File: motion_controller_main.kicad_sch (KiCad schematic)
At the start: 321 parts, among them J1 Conn_01x03_Pin, J10 H3, J11 EN4, J12 H4, J13 EN5, J14 H5, J15 EN6, J16 H6, J17 EN7, J18 H7, J19 EN5, J2 EMERGENCY, J20 H5, J21 EN6, J22 H6, J23 EN7, J24 H7, J25 H7, J26 H7, J27 H7, J28 H7, J29 Conn_01x04_Pin, J3 EN0, J30 Conn_01x04_Pin, J31 Conn_01x04_Pin, J32 Conn_01x04_Pin, J33 Conn_01x04_Pin, J34 Conn_01x04_Pin, J35 Conn_01x04_Pin, J36 Conn_01x04_Pin, J37 Conn_01x04_Pin, J38 Conn_01x04_Pin, J39 Conn_01x04_Pin, J4 H0, J40 Conn_01x04_Pin, J41 Conn_01x04_Pin, J42 Conn_01x04_Pin, J43 Conn_01x04_Pin, J44 Conn_01x04_Pin, J45 Conn_01x04_Pin, J46 Conn_01x04_Pin, J47 EMERGENCY, J48 ST-LINK, J49 Inverter, J5 EN1, J50 Conn_01x04_Pin, J51 Conn_01x03_Female, J52 EN5, J53 EN5, J54 Inverter, J55 Conn_01x12_Pin, J57 Conn_01x12_Pin, J58 Conn_01x02_Pin, J59 Conn_01x03_Pin, J6 H1, J60 Conn_01x04_Pin, J7 EN2, J8 H2, J9 EN3, Q1 BCX56, SW3 SW_Push_Dual_x2, SW4 SW_Push_Dual_x2, U1 SN65HVD232D, U10 TLP291-4, U11 TLP291-4, U12 TLP291-4, U13 TLP291-4, U14 TLP291-4, U15 TLP291-4, U16 TLP291-4, U17 ISO7741, U18 ISO7741, U19 ISO7741, U2 STM32F407IGTx, U20 ISO7741, U21 ISO7741, U3 MX25R3235FM2xx1, U30 TLP2372, U31 TLP291, U32 TLP2372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

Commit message: 250806
배선 재배치 + adc + 로드셀 보드 통합 등
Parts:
- removed C51, C52, C53, C54, C55, C56: 1nF, Capacitor_SMD:C_0603_1608Metric_Pad1.08x0.95mm_HandSolder, symbol Device:C
- removed D18, D19, D21, D22, D23: LED, LED_SMD:LED_0805_2012Metric_Pad1.15x1.40mm_HandSolder, symbol Device:LED
- removed J49, J54: Inverter, Connector_Molex:Molex_SPOX_5267-02A_1x02_P2.50mm_Vertical, symbol Connector:Conn_01x02_Pin
- removed J50, J60: Conn_01x04_Pin, Connector_Molex:Molex_SPOX_5267-04A_1x04_P2.50mm_Vertical, symbol Connector:Conn_01x04_Pin
- removed J52, J53: EN5, Connector_Molex:Molex_SPOX_5267-05A_1x05_P2.50mm_Vertical, symbol Connector:Conn_01x05_Pin
- removed J55, J57: Conn_01x12_Pin, Connector_PinHeader_2.54mm:PinHeader_1x12_P2.54mm_Vertical, symbol Connector:Conn_01x12_Pin
- removed JP2, JP3, JP4, JP5, JP6, JP7, JP8, JP9: SolderJumper_2_Open, Jumper:SolderJumper-2_P1.3mm_Open_TrianglePad1.0x1.5mm, symbol Jumper:SolderJumper_2_Open
- removed U22, U23, U24, U25, U26: ~, TMC5160:TMC5160-BOB, symbol tmc5160:tmc5160-bob
- removed U27, U28, U29: ~, TMC5160:TMC5160-CUSTOM, symbol tmc5160:tmc5160-custom
- removed U43: MAX3232, Package_SO:SOIC-16_3.9x9.9mm_P1.27mm, symbol Interface_UART:MAX3232
- added C47, C51, C52, C53, C54, C55, C56: C_Polarized_US, Capacitor_THT:CP_Radial_D8.0mm_P5.00mm, symbol Device:C_Polarized_US
- added C69, C70, C71, C73, C75, C76, C77, C79, C81: 0.1uF, Capacitor_SMD:C_0603_1608Metric, symbol Device:C
- added C72, C78: MF473K, Capacitor_THT:C_Axial_L3.8mm_D2.6mm_P12.50mm_Horizontal, symbol Device:C
- added C74, C80: 1uF, Capacitor_SMD:C_0603_1608Metric, symbol Device:C
- added C82, C83: 0.1uF, Capacitor_SMD:C_0603_1608Metric_Pad1.08x0.95mm_HandSolder, symbol Device:C
- added C84: 2.2uF, Capacitor_Tantalum_SMD:CP_EIA-3216-18_Kemet-A, symbol Device:C_Polarized_US
- added C85, C86: 4.7uF, Capacitor_SMD:C_0603_1608Metric, symbol Device:C
- added D18, D19, D21: M7, Diode_SMD:D_SMA, symbol pspice:DIODE
- added FB1: 600ohm, Inductor_SMD:L_0603_1608Metric, symbol Device:FerriteBead
- added H3, H6, H7, H8, H9: MountingHole, MountingHole:MountingHole_3.2mm_M3, symbol Mechanical:MountingHole
- added IC1: ADM3251EARWZ, SOIC127P1032X265-20N, symbol ADM3251EARWZ:ADM3251EARWZ
- added IC2, IC3: ADS8321E_250, ADS8321:SOP65P490X110-8N, symbol ADS8321E_250:ADS8321E_250
- added J49, J54, J70, J71: Conn_01x03_Pin, Connector_Molex:Molex_SPOX_5267-03A_1x03_P2.50mm_Vertical, symbol Connector:Conn_01x03_Pin
- added J50, J60, J66, J67: EN3, Connector_Molex:Molex_SPOX_5267-05A_1x05_P2.50mm_Vertical, symbol Connector:Conn_01x05_Pin
- added J52, J65: LOADCELL, connectors:SMW250-5, symbol Connector:Conn_01x05_Socket
- added J53, J64: CON2, Connector_Molex:Molex_SPOX_5267-02A_1x02_P2.50mm_Vertical, symbol Connector:Conn_01x02_Pin
- added J55: LOADCELL PWR, connectors:ECH381R-2P, symbol Connector:Conn_01x02_Pin
- added J56, J57, J61, J62, J63, J68: Conn_01x04_Pin, connectors:ECH381R-4P, symbol Connector:Conn_01x04_Pin
- added J69: Conn_01x07_Pin, Connector_PinHeader_2.54mm:PinHeader_1x07_P2.54mm_Vertical, symbol Connector:Conn_01x07_Pin
- added L1: 10uH, Capacitor_SMD:C_1812_4532Metric, symbol Device:L
- added L2: 4.7uH, Inductor_SMD:L_1210_3225Metric, symbol Device:L
- added PS1: NXJ1S0303MC-R13, NXJ1S0303MCR13, symbol NXJ1S0303MC-R13:NXJ1S0303MC-R13
- added Q2, Q3: BCX56, Package_TO_SOT_SMD:SOT-89-3, symbol Transistor_BJT:BCX56
- added R113, R115, R122, R124: 100K 0.1%, Resistor_SMD:R_0805_2012Metric_Pad1.20x1.40mm_HandSolder, symbol Device:R
- added R114, R123: 500 0.1%, Resistor_SMD:R_0805_2012Metric_Pad1.20x1.40mm_HandSolder, symbol Device:R
- added R116, R117, R118, R119, R125, R126, R127, R128: 100 0.1%, Resistor_SMD:R_0603_1608Metric_Pad0.98x0.95mm_HandSolder, symbol Device:R
- added R120, R129: 5, Resistor_SMD:R_0603_1608Metric_Pad0.98x0.95mm_HandSolder, symbol Device:R
- added R121, R130: 100K, Resistor_SMD:R_0603_1608Metric_Pad0.98x0.95mm_HandSolder, symbol Device:R
- added R131, R132, R138, R140, R142, R144, R146, R148, R150, R152, R154, R156, R158, R160: 330, Resistor_SMD:R_0603_1608Metric_Pad0.98x0.95mm_HandSolder, symbol Device:R
- added R133, R134, R137, R139, R141, R143, R145, R147, R149, R151, R153, R155, R157, R159: 1.2k, Resistor_SMD:R_1206_3216Metric, symbol Device:R
- added R135, R136: 4.7K, Resistor_SMD:R_0603_1608Metric_Pad0.98x0.95mm_HandSolder, symbol Device:R
- added R161: 500, Resistor_SMD:R_0805_2012Metric_Pad1.20x1.40mm_HandSolder, symbol Device:R
- added U22, U23, U24, U25, U26, U27, U28, U29, U35, U44, U52: ~, TMC5160:TMC5160-ADT, symbol tmc5160:tmc5160-adt
- added U43, U45: AD8606ARZ, Package_SO:SOIC-8_3.9x4.9mm_P1.27mm, symbol Amplifier_Operational:NCS2325DM
- added U46: ~, Relay_THT:Relay_DPDT_AXICOM_IMSeries_Pitch3.2mm, symbol relay:AGN20012
- added U47: ISO7741, Package_SO:SOIC-16W_7.5x10.3mm_P1.27mm, symbol Isolator:Si8641BC-B-IS1
- added U48, U49, U50: TLP291-4, Package_SO:SOIC-16_4.55x10.3mm_P1.27mm, symbol Isolator:TLP291-4
- added U51: MIC5205-5.0YM5, Package_TO_SOT_SMD:SOT-23-5, symbol Regulator_Linear:MIC5205-5.0YM5
- added X2: TXC-7C, sunny-sco-10:sunny-sco-10, symbol Oscillator:TXC-7C
- C57: value 1nF -> 22uF; footprint Capacitor_SMD:C_0603_1608Metric_Pad1.08x0.95mm_HandSolder -> Capacitor_SMD:C_0805_2012Metric
- C58: value 1nF -> 22pF; footprint Capacitor_SMD:C_0603_1608Metric_Pad1.08x0.95mm_HandSolder -> Capacitor_SMD:C_0603_1608Metric
- C59: value 1nF -> 0.1uF; footprint Capacitor_SMD:C_0603_1608Metric_Pad1.08x0.95mm_HandSolder -> Capacitor_SMD:C_0603_1608Metric
- C60, C61, C62: value 1nF -> 0.1uF 16v; footprint Capacitor_SMD:C_0603_1608Metric_Pad1.08x0.95mm_HandSolder -> Capacitor_SMD:C_0603_1608Metric
- C64: value 0.1uF -> 0.1uF 10v; footprint Capacitor_SMD:C_0603_1608Metric_Pad1.08x0.95mm_HandSolder -> Capacitor_SMD:C_0603_1608Metric
- C65, C66, C67, C68: footprint Capacitor_SMD:C_0603_1608Metric_Pad1.08x0.95mm_HandSolder -> Capacitor_SMD:C_0603_1608Metric
- J47: value EMERGENCY -> SOLVALVE MAIN
- J51: footprint connectors:ECH381R-3P -> Connector_Molex:Molex_SPOX_5267-03A_1x03_P2.50mm_Vertical
- Y1: footprint Crystal:Crystal_HC52-6mm_Vertical -> sunny-sco-10:HC-49SMD
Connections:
- net PA0 is gone; now on net EA0: U2.40 (PA0)
- net PA1 is gone; now on net EB0: U2.41 (PA1)
- net PA2 is gone; now on net EZ0: U2.42 (PA2)
- net +12V: now also J50.2 (Pin_2), J60.2 (Pin_2), J66.2 (Pin_2), J67.2 (Pin_2), R137.2, R139.2, R141.2, R143.2, R145.2, R147.2, R149.2, R151.2, R153.2, R155.2, R157.2, R159.2
- net +24V: now also U36.2 (NC1), R133.2, R134.2, U22.15 (12V), U22.16 (12V), U23.15 (12V), U23.16 (12V), U24.15 (12V), U24.16 (12V), U25.15 (12V), U25.16 (12V), U26.15 (12V), U26.16 (12V), U27.15 (12V), U27.16 (12V), U28.15 (12V), U28.16 (12V), U29.15 (12V), U29.16 (12V), U35.15 (12V), U35.16 (12V), U44.15 (12V), U44.16 (12V), U46.2 (NC1), U46.7 (NC2), U52.15 (12V), U52.16 (12V)
- net +3.3V: now also C24.2, C59.1, R104.1, C83.2, IC1.2 (VCC_1), IC1.3 (VCC_2), J69.1 (Pin_1), J70.2 (Pin_2), J71.2 (Pin_2), L1.1, R136.1, R138.2, R140.2, R142.2, R144.2, R146.2, R148.2, R150.2, R152.2, R154.2, R156.2, R158.2, R160.2, U47.16 (VDD2); no longer C23.2, C65.1, J47.2 (Pin_2), R103.1
- net +3.3VP: now also C82.2, R135.2, U22.3 (3V3), U22.4 (3V3), U23.3 (3V3), U23.4 (3V3), U24.3 (3V3), U24.4 (3V3), U25.3 (3V3), U25.4 (3V3), U26.3 (3V3), U26.4 (3V3), U27.3 (3V3), U27.4 (3V3), U28.3 (3V3), U28.4 (3V3), U29.3 (3V3), U29.4 (3V3), U35.3 (3V3), U35.4 (3V3), U44.3 (3V3), U44.4 (3V3), U47.1 (VDD1), U52.3 (3V3), U52.4 (3V3), X2.1 (EN), X2.4 (Vdd); no longer U36.4 (NO1)
- net A1_0: now also J41.3 (Pin_3), J42.2 (Pin_2), U22.27 (A1), U22.28 (A1); no longer J41.2 (Pin_2), J42.3 (Pin_3)
- net A1_1: now also U23.27 (A1), U23.28 (A1); no longer C57.2
- net A1_2: now also U24.27 (A1), U24.28 (A1); no longer C61.2
- net A2_0: now also J41.4 (Pin_4), J42.1 (Pin_1), U22.29 (A2), U22.30 (A2); no longer J41.1 (Pin_1), J42.4 (Pin_4)
- net A2_1: now also U23.29 (A2), U23.30 (A2); no longer C58.2
- net A2_2: now also U24.29 (A2), U24.30 (A2); no longer C62.2
- net ADC_CS0: now also U2.128 (PH13); no longer U2.131 (PI0)
- net ADC_CS0_O: now also IC2.5 (~{CS}/SHDN)
- net ADC_CS1: now also U2.129 (PH14); no longer U2.128 (PH13)
- net ADC_CS1_O: now also IC3.5 (~{CS}/SHDN)
- net B1_0: now also J41.1 (Pin_1), J42.4 (Pin_4), U22.23 (B1), U22.24 (B1); no longer J41.4 (Pin_4), J42.1 (Pin_1)
- net B1_1: now also U23.23 (B1), U23.24 (B1)
- net B1_2: now also U24.23 (B1), U24.24 (B1); no longer C59.2
- net B2_0: now also J41.2 (Pin_2), J42.3 (Pin_3), U22.25 (B2), U22.26 (B2); no longer J41.3 (Pin_3), J42.2 (Pin_2)
- net B2_1: now also U23.25 (B2), U23.26 (B2)
- net B2_2: now also U24.25 (B2), U24.26 (B2); no longer C60.2
- net BUZZER: now also U2.8 (PC13); no longer U2.50 (PA4)
- net CAN1H: now also J49.3 (Pin_3), J54.3 (Pin_3)
- net CAN1L: now also J49.2 (Pin_2), J54.2 (Pin_2)
- net CS0: now also U2.175 (PI6), U47.11 (B4); no longer U18.5 (A3), U2.1 (PE2)
- net CS0_O: now also U22.1 (CSN), U47.6 (A4), U52.1 (CSN); no longer U18.12 (B3)
- net CS1: now also U19.11 (B4), U2.169 (PE0); no longer U18.4 (A2), U2.4 (PE5)
- net CS1_O: now also U19.6 (A4), U23.1 (CSN); no longer U18.13 (B2)
- net CS2: now also U2.154 (PG11); no longer U2.8 (PC13)
- net CS2_O: now also U24.1 (CSN)
- net CS3: now also U18.4 (A2), U2.153 (PG10); no longer U2.173 (PI4), U20.3 (A1)
- net CS3_O: now also U18.13 (B2), U25.1 (CSN); no longer U20.14 (B1)
- net CS4: now also U18.5 (A3), U2.152 (PG9); no longer U2.168 (PB9), U20.4 (A2)
- net CS4_O: now also U18.12 (B3), U26.1 (CSN); no longer U20.13 (B2)
- net CS5: now also U2.150 (PD6), U20.3 (A1); no longer U2.164 (PB6), U20.5 (A3)
- net CS5_O: now also U20.14 (B1), U27.1 (CSN); no longer U20.12 (B3)
- net CS6: now also U2.146 (PD4), U20.4 (A2); no longer U17.5 (A3), U2.156 (PG13)
- net CS6_O: now also U20.13 (B2), U28.1 (CSN); no longer U17.12 (B3)
- net CS7: now also U2.145 (PD3), U20.5 (A3); no longer U2.153 (PG10), U21.11 (B4)
- net CS7_O: now also U20.12 (B3), U29.1 (CSN); no longer U21.6 (A4)
- net DIAG0_0: now also U2.174 (PI5), U47.12 (B3); no longer U19.12 (B3), U2.47 (PA3)
- net DIAG0_0_O: now also U22.2 (DIAG0), U47.5 (A3); no longer D16.2 (A), U19.5 (A3)
- net DIAG0_1: now also U2.173 (PI4), U47.13 (B2); no longer U19.13 (B2), U2.46 (PH5)
- net DIAG0_1_O: now also U23.2 (DIAG0), U47.4 (A2); no longer D17.2 (A), U19.4 (A2)
- net DIAG0_2: now also U19.12 (B3), U2.168 (PB9); no longer U19.14 (B1), U2.45 (PH4)
- net DIAG0_2_O: now also U19.5 (A3), U24.2 (DIAG0); no longer U19.3 (A1)
- net DIAG0_3: now also U19.13 (B2), U2.167 (PB8); no longer U2.146 (PD4), U21.14 (B1)
- net DIAG0_3_O: now also U19.4 (A2), U25.2 (DIAG0); no longer U21.3 (A1)
- net DIAG0_4: now also U19.14 (B1), U2.155 (PG12); no longer U2.147 (PD5), U21.13 (B2)
- net DIAG0_4_O: now also U19.3 (A1), U26.2 (DIAG0); no longer D20.2 (A), U21.4 (A2)
- net DIAG0_5: now also U18.6 (A4), U2.151 (PD7); no longer U2.150 (PD6), U21.12 (B3)
- net DIAG0_5_O: now also U18.11 (B4), U27.2 (DIAG0); no longer U21.5 (A3)
- net DIAG0_6: now also U2.143 (PD1); no longer U2.151 (PD7)
- net DIAG0_6_O: now also U28.2 (DIAG0)
- net DIAG0_7: now also U2.141 (PC12), U21.12 (B3); no longer U18.6 (A4), U2.152 (PG9)
- net DIAG0_7_O: now also U21.5 (A3), U29.2 (DIAG0); no longer U18.11 (B4)
- net DRV_ENN_O: now also U22.10 (DRV_ENN), U23.10 (DRV_ENN), U24.10 (DRV_ENN), U25.10 (DRV_ENN), U26.10 (DRV_ENN), U27.10 (DRV_ENN), U28.10 (DRV_ENN), U29.10 (DRV_ENN), U35.10 (DRV_ENN), U44.10 (DRV_ENN), U52.10 (DRV_ENN); no longer U36.3 (COM1)
- net EA0: no longer U2.54 (PC4)
- net EB0: no longer U2.55 (PC5)
- net EMERGENCY: now also U2.176 (PI7); no longer U2.174 (PI5)
- net EZ0: no longer U2.56 (PB0)
- net GND: now also C24.1, C57.1, C59.2, C83.1, IC1.10 (GND_5), IC1.4 (GND_1), IC1.5 (GND_2), IC1.6 (GND_3), IC1.7 (GND_4), J49.1 (Pin_1), J54.1 (Pin_1), J69.2 (Pin_2), J70.1 (Pin_1), J71.1 (Pin_1), PS1.1 (-VIN), U47.15 (GND2), U47.9 (GND2), U48.11, U48.13, U48.15, U48.9, U49.11, U49.13, U49.15, U49.9, U50.11, U50.13, U50.15, U50.9; no longer C23.1, C65.2, C67.2, C68.2, J47.1 (Pin_1), J59.3 (Pin_3)
- net GND1: now also J50.1 (Pin_1), J60.1 (Pin_1), J66.1 (Pin_1), J67.1 (Pin_1), U48.2, U48.4, U48.6, U48.8, U49.2, U49.4, U49.6, U49.8, U50.2, U50.4, U50.6, U50.8
- net GND2: now also J47.2 (Pin_2), U36.4 (NO1), C47.2, C51.2, C52.2, C53.2, C54.2, C55.2, C56.2, C82.1, D21.1 (K), Q2.3 (E), Q3.3 (E), U22.11 (GND), U22.12 (GND), U22.13 (GND), U22.14 (GND), U22.8 (GND), U23.11 (GND), U23.12 (GND), U23.13 (GND), U23.14 (GND), U23.6 (CLK16), U23.8 (GND), U24.11 (GND), U24.12 (GND), U24.13 (GND), U24.14 (GND), U24.6 (CLK16), U24.8 (GND), U25.11 (GND), U25.12 (GND), U25.13 (GND), U25.14 (GND), U25.6 (CLK16), U25.8 (GND), U26.11 (GND), U26.12 (GND), U26.13 (GND), U26.14 (GND), U26.6 (CLK16), U26.8 (GND), U27.11 (GND), U27.12 (GND), U27.13 (GND), U27.14 (GND), U27.6 (CLK16), U27.8 (GND), U28.11 (GND), U28.12 (GND), U28.13 (GND), U28.14 (GND), U28.6 (CLK16), U28.8 (GND), U29.11 (GND), U29.12 (GND), U29.13 (GND), U29.14 (GND), U29.6 (CLK16), U29.8 (GND), U35.11 (GND), U35.12 (GND), U35.13 (GND), U35.14 (GND), U35.6 (CLK16), U35.8 (GND), U44.11 (GND), U44.12 (GND), U44.13 (GND), U44.14 (GND), U44.6 (CLK16), U44.8 (GND), U46.4 (NO1), U46.5 (NO2), U46.8 (-), U47.2 (GND1), U47.8 (GND1), U52.11 (GND), U52.12 (GND), U52.13 (GND), U52.14 (GND), U52.8 (GND), X2.2 (GND); no longer C57.1, C58.1, C59.1, C60.1, C61.1, C62.1, U36.2 (NC1)
- net GNDS: now also C23.1, D20.1 (K), C73.2, C74.2, C75.2, C79.2, C80.2, C81.2, C84.2, C85.1, C86.2, IC2.4 (GND), IC3.4 (GND), J52.1 (Pin_1), J55.1 (Pin_1), J65.1 (Pin_1), R119.2, R121.2, R128.2, R130.2, U43.4 (V-), U45.4 (V-), U51.2 (GND); no longer C24.1
- net INVERTER0: now also D17.2 (A); no longer U38.1
- net INVERTER1: now also D16.2 (A), U2.131 (PI0); no longer U2.129 (PH14), U41.1
- net RS232_RX: now also IC1.15 (RIN)
- net RS232_TX: now also IC1.16 (TOUT)
- net SPI2_MISO_O: now also IC2.6 (DOUT), IC3.6 (DOUT)
- net SPI2_SCK_O: now also IC2.7 (DCLOCK), IC3.7 (DCLOCK)
- net SPI3_MISO_O: now also U22.5 (MISO), U23.5 (MISO), U24.5 (MISO), U25.5 (MISO), U26.5 (MISO), U27.5 (MISO), U28.5 (MISO), U29.5 (MISO), U35.5 (MISO), U44.5 (MISO), U52.5 (MISO)
- net SPI3_MOSI_O: now also U22.7 (MOSI), U23.7 (MOSI), U24.7 (MOSI), U25.7 (MOSI), U26.7 (MOSI), U27.7 (MOSI), U28.7 (MOSI), U29.7 (MOSI), U35.7 (MOSI), U44.7 (MOSI), U52.7 (MOSI)
- net SPI3_SCK_O: now also U22.9 (SCK), U23.9 (SCK), U24.9 (SCK), U25.9 (SCK), U26.9 (SCK), U27.9 (SCK), U28.9 (SCK), U29.9 (SCK), U35.9 (SCK), U44.9 (SCK), U52.9 (SCK)
- net USART1_RX: now also IC1.8 (ROUT)
- net USART1_TX: now also IC1.9 (TIN)
- net VPP: now also C47.1, C51.1, C52.1, C53.1, C54.1, C55.1, C56.1, U22.17 (60V), U22.18 (60V), U22.19 (60V), U22.20 (60V), U22.21 (60V), U22.22 (60V), U23.17 (60V), U23.18 (60V), U23.19 (60V), U23.20 (60V), U23.21 (60V), U23.22 (60V), U24.17 (60V), U24.18 (60V), U24.19 (60V), U24.20 (60V), U24.21 (60V), U24.22 (60V), U25.17 (60V), U25.18 (60V), U25.19 (60V), U25.20 (60V), U25.21 (60V), U25.22 (60V), U26.17 (60V), U26.18 (60V), U26.19 (60V), U26.20 (60V), U26.21 (60V), U26.22 (60V), U27.17 (60V), U27.18 (60V), U27.19 (60V), U27.20 (60V), U27.21 (60V), U27.22 (60V), U28.17 (60V), U28.18 (60V), U28.19 (60V), U28.20 (60V), U28.21 (60V), U28.22 (60V), U29.17 (60V), U29.18 (60V), U29.19 (60V), U29.20 (60V), U29.21 (60V), U29.22 (60V), U35.17 (60V), U35.18 (60V), U35.19 (60V), U35.20 (60V), U35.21 (60V), U35.22 (60V), U44.17 (60V), U44.18 (60V), U44.19 (60V), U44.20 (60V), U44.21 (60V), U44.22 (60V), U52.17 (60V), U52.18 (60V), U52.19 (60V), U52.20 (60V), U52.21 (60V), U52.22 (60V)
- net B1_3: now reaches J31.1 (Pin_1)
- net B1_3: now also J32.4 (Pin_4), U25.23 (B1), U25.24 (B1); no longer J40.4 (Pin_4)
- net B2_3: now reaches J31.2 (Pin_2)
- net B2_3: now also J32.3 (Pin_3), U25.25 (B2), U25.26 (B2); no longer J40.3 (Pin_3)
- net A1_3: now reaches J31.3 (Pin_3)
- net A1_3: now also J32.2 (Pin_2), U25.27 (A1), U25.28 (A1); no longer J40.2 (Pin_2)
- net A2_3: now reaches J31.4 (Pin_4)
- net A2_3: now also J32.1 (Pin_1), U25.29 (A2), U25.30 (A2); no longer J40.1 (Pin_1)
- net at U40.10 (EN2): now also R103.2; no longer R104.2
- net at U40.7 (EN1): now also R104.2; no longer R103.2
- net B1_4: now reaches J34.4 (Pin_4)
- net B1_4: now also J33.1 (Pin_1), U26.23 (B1), U26.24 (B1); no longer J37.1 (Pin_1)
- net B2_4: now reaches J34.3 (Pin_3)
- net B2_4: now also J33.2 (Pin_2), U26.25 (B2), U26.26 (B2); no longer J37.2 (Pin_2)
- net A1_4: now reaches J34.2 (Pin_2)
- net A1_4: now also J33.3 (Pin_3), U26.27 (A1), U26.28 (A1); no longer J37.3 (Pin_3)
- net A2_4: now reaches J34.1 (Pin_1)
- net A2_4: now also J33.4 (Pin_4), U26.29 (A2), U26.30 (A2); no longer J37.4 (Pin_4)
- net EB12: now reaches U2.13 (PI11)
- net EB12: now also R146.1, U49.16
- net DIAG0_9: now reaches U2.139 (PC10)
- net DIAG0_9: now also U21.14 (B1)
- net DIAG0_8: now reaches U2.140 (PC11)
- net DIAG0_8: now also U21.13 (B2)
- net CS9: now reaches U2.142 (PD0)
- net CS9: now also U21.11 (B4)
- net CS8: now reaches U2.144 (PD2)
- net CS8: now also U17.5 (A3)
- net DIAG0_11: now reaches U2.170 (PE1)
- net DIAG0_11: now also U47.14 (B1)
- net PE3: now reaches U2.2 (PE3)
- net PE3: now also J69.4 (Pin_4)
- net PE4: now reaches U2.3 (PE4)
- net PE4: now also J69.5 (Pin_5)
- net PE6: now reaches U2.5 (PE6)
- net PE6: now also J69.7 (Pin_7)
- net EMERGENCY_O: now reaches J2.1 (Pin_1), U36.1 (+)
- net EMERGENCY_O: now also U46.1 (+)
- net B1_7: now reaches J39.1 (Pin_1)
- net B1_7: now also J40.4 (Pin_4), U29.23 (B1), U29.24 (B1); no longer J32.4 (Pin_4)
- net B2_7: now reaches J39.2 (Pin_2)
- net B2_7: now also J40.3 (Pin_3), U29.25 (B2), U29.26 (B2); no longer J32.3 (Pin_3)
- net A1_7: now reaches J39.3 (Pin_3)
- net A1_7: now also J40.2 (Pin_2), U29.27 (A1), U29.28 (A1); no longer J32.2 (Pin_2)
- net A2_7: now reaches J39.4 (Pin_4)
- net A2_7: now also J40.1 (Pin_1), U29.29 (A2), U29.30 (A2); no longer J32.1 (Pin_1)
- net at U41.3: now also Q2.1 (B)
- net at U41.4: now also R133.1
- net at U38.3: now also Q3.1 (B)
- net at U38.4: now also R134.1
- net at C64.1: now also IC1.19 (V+)
- net +3.3ISO: now reaches C64.2
- net +3.3ISO: now also C58.2, C65.2, IC1.20 (VISO), L2.2
- net at D16.1 (K): now also R131.2
- net at D17.1 (K): now also R132.2
- net B1_6: now reaches J38.4 (Pin_4)
- net B1_6: now also J37.1 (Pin_1), U28.23 (B1), U28.24 (B1); no longer J33.1 (Pin_1)
- net B2_6: now reaches J38.3 (Pin_3)
- net B2_6: now also J37.2 (Pin_2), U28.25 (B2), U28.26 (B2); no longer J33.2 (Pin_2)
- net A1_6: now reaches J38.2 (Pin_2)
- net A1_6: now also J37.3 (Pin_3), U28.27 (A1), U28.28 (A1); no longer J33.3 (Pin_3)
- net A2_6: now reaches J38.1 (Pin_1)
- net A2_6: now also J37.4 (Pin_4), U28.29 (A2), U28.30 (A2); no longer J33.4 (Pin_4)
- net B1_5: now reaches J35.1 (Pin_1), J36.4 (Pin_4)
- net B1_5: now also U27.23 (B1), U27.24 (B1)
- net B2_5: now reaches J35.2 (Pin_2), J36.3 (Pin_3)
- net B2_5: now also U27.25 (B2), U27.26 (B2)
- net A1_5: now reaches J35.3 (Pin_3), J36.2 (Pin_2)
- net A1_5: now also U27.27 (A1), U27.28 (A1)
- net A2_5: now reaches J35.4 (Pin_4), J36.1 (Pin_1)
- net A2_5: now also U27.29 (A2), U27.30 (A2)
- net at C67.1: now also C77.1, R123.1, R124.2, U45.6 (-)
- net at C66.2: now also C76.2, R122.1, R123.2, U45.2 (-)
- net at C66.1: now also C76.1, R122.2, R125.1, U45.1
- net at C68.1: now also C70.1, R113.2, R116.1, U43.1
- removed net +3V3: C24.2, R104.1, U40.16 (VDD2)
- net PC14 renamed EZ11
- net EZ11: now also R138.1, U48.16
- net PC15 renamed EB11
- net EB11: now also R140.1, U48.14
- net PF0 renamed EA12
- net EA12: now also R148.1, U49.14
- net PF1: no longer names the net of U2.17 (PF1)
- net PF10 renamed EA14
- net EA14: now also R160.1, U50.10
- net PF2 renamed EZ13
- net EZ13: now also R150.1, U49.12
- net PF3 renamed EB13
- net EB13: now also R152.1, U49.10
- net PF4 renamed EA13
- net EA13: now also R154.1, U50.16
- net PF5: no longer names the net of U2.21 (PF5)
- net PF6: no longer names the net of U2.24 (PF6)
- net PF7: no longer names the net of U2.25 (PF7)
- net PF8 renamed EZ14
- net EZ14: now also R156.1, U50.14
- net PF9 renamed EB14
- net EB14: now also R158.1, U50.12
- net PH2: no longer names the net of U2.43 (PH2)
- net PH3: no longer names the net of U2.44 (PH3)
- net PI10 renamed EZ12
- net EZ12: now also R144.1, U48.10
- net PI9 renamed EA11
- net EA11: now also R142.1, U48.12
- new net: C81.1, J52.5 (Pin_5), R130.1
- new net: D18.1 (K), J53.1 (Pin_1), Q2.2 (C)
- new net: C78.2, IC3.2 (+IN), R125.2
- new net: C74.1, IC2.8 (+VCC), R120.2
- new net: C69.1, C71.1, R114.1, R115.2, U43.6 (-)
- new net: C69.2, C71.2, R115.1, R117.1, U43.7
- new net: C67.2, C77.2, R124.1, R126.1, U45.7
- new net: C68.2, C70.2, R113.1, R114.2, U43.2 (-)
- new net: C72.1, IC2.3 (-IN), R117.2
- new net: C80.1, IC3.8 (+VCC), R129.2
- new net: C78.1, IC3.3 (-IN), R126.2
- new net: C60.1, IC1.18 (C1+)
- new net: C60.2, IC1.17 (C1-)
- new net: D19.1 (K), J64.1 (Pin_1), Q3.2 (C)
- new net: R136.2, U47.10 (EN2)
- new net: R135.1, U47.7 (EN1)
- new net: R132.1, U38.1
- new net: C72.2, IC2.2 (+IN), R116.2
- new net: C79.1, IC3.1 (VREF), R127.2, R128.1
- new net: C73.1, IC2.1 (VREF), R118.2, R119.1
- new net: C57.2, L1.2, PS1.3 (+VIN)
- new net: L2.1, PS1.8 (+VOUT)
- new net: C86.1, FB1.2, U51.1 (IN)
- new net: D20.2 (A), R161.1
- new net: R131.1, U41.1
- new net: C62.1, IC1.12 (V-)
- new net: C61.2, IC1.13 (C2-)
- new net: C61.1, IC1.14 (C2+)
- new net: C85.2, U51.4 (BP)
- new net: C75.1, J65.5 (Pin_5), R121.1
- new net +5V: C23.2, C84.1, J52.2 (Pin_2), J65.2 (Pin_2), R103.1, R118.1, R120.1, R127.1, R129.1, R161.2, U40.16 (VDD2), U43.8 (V+), U45.8 (V+), U51.5 (OUT)
- new net +5V5: FB1.1, J55.2 (Pin_2), U51.3 (EN)
- new net 16MHz: U22.6 (CLK16), U52.6 (CLK16), X2.3 (OUT)
- new net A1_11: J57.3 (Pin_3), J68.2 (Pin_2), U52.27 (A1), U52.28 (A1)
- new net A1_8: J56.3 (Pin_3), J61.2 (Pin_2), U35.27 (A1), U35.28 (A1)
- new net A1_9: J62.3 (Pin_3), J63.2 (Pin_2), U44.27 (A1), U44.28 (A1)
- new net A2_11: J57.4 (Pin_4), J68.1 (Pin_1), U52.29 (A2), U52.30 (A2)
- new net A2_8: J56.4 (Pin_4), J61.1 (Pin_1), U35.29 (A2), U35.30 (A2)
- new net A2_9: J62.4 (Pin_4), J63.1 (Pin_1), U44.29 (A2), U44.30 (A2)
- new net ADC1_IN14: J71.3 (Pin_3), U2.54 (PC4)
- new net ADC1_IN15: J70.3 (Pin_3), U2.55 (PC5)
- new net B1_11: J57.1 (Pin_1), J68.4 (Pin_4), U52.23 (B1), U52.24 (B1)
- new net B1_8: J56.1 (Pin_1), J61.4 (Pin_4), U35.23 (B1), U35.24 (B1)
- new net B1_9: J62.1 (Pin_1), J63.4 (Pin_4), U44.23 (B1), U44.24 (B1)
- new net B2_11: J57.2 (Pin_2), J68.3 (Pin_3), U52.25 (B2), U52.26 (B2)
- new net B2_8: J56.2 (Pin_2), J61.3 (Pin_3), U35.25 (B2), U35.26 (B2)
- new net B2_9: J62.2 (Pin_2), J63.3 (Pin_3), U44.25 (B2), U44.26 (B2)
- new net CS8_O: U17.12 (B3), U35.1 (CSN)
- new net CS9_O: U21.6 (A4), U44.1 (CSN)
- new net DIAG0_11_O: U47.3 (A1), U52.2 (DIAG0)
- new net DIAG0_8_O: U21.4 (A2), U35.2 (DIAG0)
- new net DIAG0_9_O: U21.3 (A1), U44.2 (DIAG0)
- new net GND3: C58.1, C62.2, C65.1, IC1.11 (GNDISO), J59.3 (Pin_3), PS1.7 (-VOUT)
- new net INVERTER0_O: D19.2 (A), J64.2 (Pin_2), U46.6 (COM2)
- new net INVERTER1_O: D18.2 (A), J53.2 (Pin_2), U46.3 (COM1)
- new net PE2: J69.3 (Pin_3), U2.1 (PE2)
- new net PE5: J69.6 (Pin_6), U2.4 (PE5)
- new net S0+: J65.4 (Pin_4), U43.3 (+)
- new net S0-: J65.3 (Pin_3), U43.5 (+)
- new net S1+: J52.4 (Pin_4), U45.3 (+)
- new net S1-: J52.3 (Pin_3), U45.5 (+)
- new net SOLVALVE_MAIN: D21.2 (A), J47.1 (Pin_1), U36.3 (COM1)
- new net S_EA11: J50.5 (Pin_5), R141.1, U48.5
- new net S_EA12: J60.5 (Pin_5), R147.1, U49.3
- new net S_EA13: J66.5 (Pin_5), R153.1, U50.1
- new net S_EA14: J67.5 (Pin_5), R159.1, U50.7
- new net S_EB11: J50.4 (Pin_4), R139.1, U48.3
- new net S_EB12: J60.4 (Pin_4), R145.1, U49.1
- new net S_EB13: J66.4 (Pin_4), R151.1, U49.7
- new net S_EB14: J67.4 (Pin_4), R157.1, U50.5
- new net S_EZ11: J50.3 (Pin_3), R137.1, U48.1
- new net S_EZ12: J60.3 (Pin_3), R143.1, U48.7
- new net S_EZ13: J66.3 (Pin_3), R149.1, U49.5
- new net S_EZ14: J67.3 (Pin_3), R155.1, U50.3
- no-connect marks 36 -> 0
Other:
- note added: "ADC"
- note added: "RS232"
- moved on the sheet: C16, C27, C28, C29, C30, C31, C32, C33, C34, C35, C48, C49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

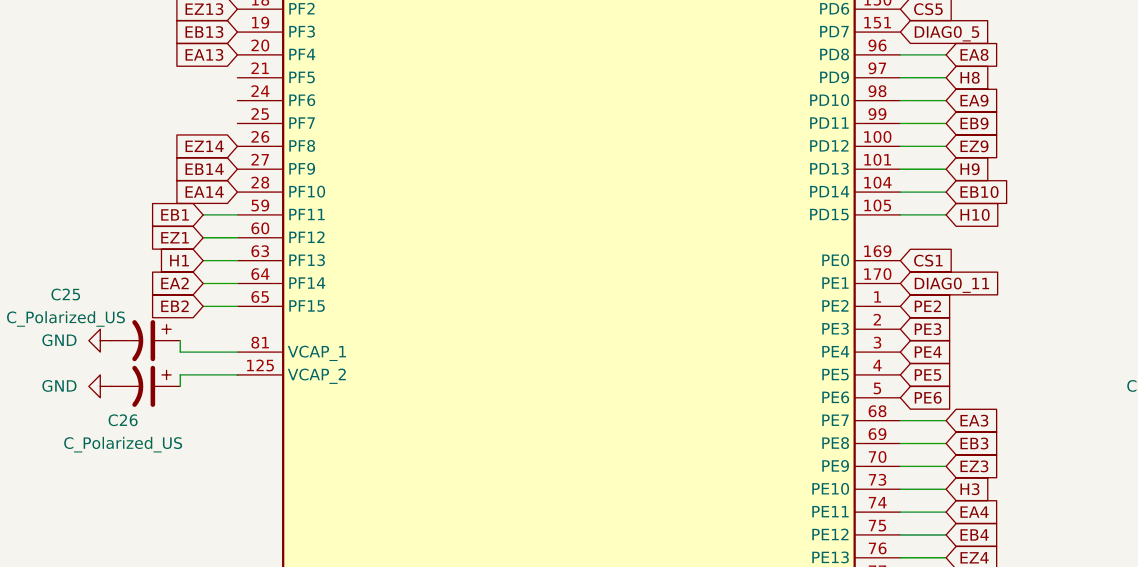
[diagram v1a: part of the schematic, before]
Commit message: 250825
E14A핀 연결 불량 처리 PE5못씀
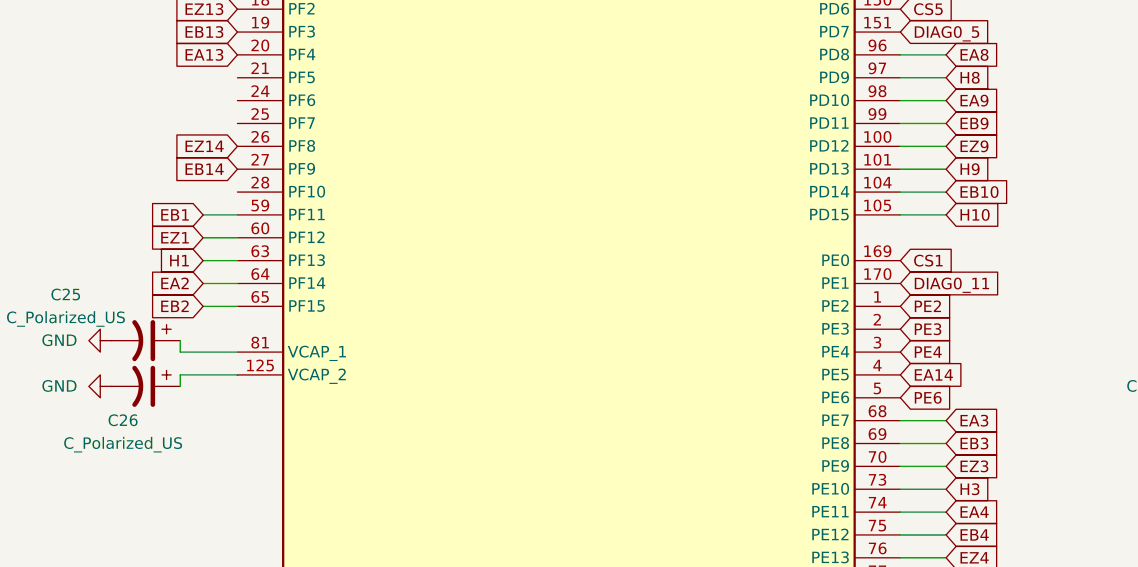
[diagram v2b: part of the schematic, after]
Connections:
- net EA14: now also U2.4 (PE5); no longer U2.28 (PF10)
- net PE5: no longer U2.4 (PE5)
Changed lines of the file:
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@@
 		)
 	)
-	(global_label "PE5"
+	(global_label "A2_8"
+		(shape input)
+		(at 819.15 699.77 0)
+		(fields_autoplaced yes)
+		(effects
+			(font
+				(size 1.27 1.27)
+			)
+			(justify left)
+		)
+		(property "Intersheetrefs" "${INTERSHEET_REFS}"
+			(at 826.6104 699.77 0)
+			(effects
+				(font
+					(size 1.27 1.27)
+				)
+				(justify left)
+				(hide yes)
+			)
+		)
+	)
+	(global_label "EA1"
+		(shape input)
+		(at 143.51 426.72 180)
+		(fields_autoplaced yes)
+		(effects
+			(font
+				(size 1.27 1.27)
+			)
+			(justify right)
+		)
+		(property "Intersheetrefs" "${INTERSHEET_REFS}"
+			(at 137.0777 426.72 0)
+			(effects
+				(font
+					(size 1.27 1.27)
+				)
+				(justify right)
+				(hide yes)
+			)
+		)
+	)
+	(global_label "EA14"
 		(shape input)
 		(at 469.9 289.56 0)
@@
 		)
 		(property "Intersheetrefs" "${INTERSHEET_REFS}"
-			(at 476.5137 289.56 0)
-			(effects
-				(font
-					(size 1.27 1.27)
-				)
-				(justify left)
-				(hide yes)
-			)
-		)
-	)
-	(global_label "A2_8"
-		(shape input)
-		(at 819.15 699.77 0)
-		(fields_autoplaced yes)
-		(effects
-			(font
-				(size 1.27 1.27)
-			)
-			(justify left)
-		)
-		(property "Intersheetrefs" "${INTERSHEET_REFS}"
-			(at 826.6104 699.77 0)
-			(effects
-				(font
-					(size 1.27 1.27)
-				)
-				(justify left)
-				(hide yes)
-			)
-		)
-	)
-	(global_label "EA1"
-		(shape input)
-		(at 143.51 426.72 180)
-		(fields_autoplaced yes)
-		(effects
-			(font
-				(size 1.27 1.27)
-			)
-			(justify right)
-		)
-		(property "Intersheetrefs" "${INTERSHEET_REFS}"
-			(at 137.0777 426.72 0)
-			(effects
-				(font
-					(size 1.27 1.27)
-				)
-				(justify right)
+			(at 477.5418 289.56 0)
+			(effects
+				(font
+					(size 1.27 1.27)
+				)
+				(justify left)
 				(hide yes)
 			)
@@
 				(hide yes)
 			)
-		)
-	)
-	(global_label "EA14"
-		(shape input)
-		(at 396.24 269.24 180)
-		(fields_autoplaced yes)
-		(effects
-			(font
-				(size 1.27 1.27)
-			)
-			(justify right)
-		)
-		(property "Intersheetrefs" "${INTERSHEET_REFS}"
-			(at 388.5982 269.24 0)
-			(effects
-				(font
-					(size 1.27 1.27)
-				)
-				(justify right)
-				(hide yes)
-			)

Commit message: 251022
gpio확인 pe5가 없어서 커넥터 수정
무라타 보드에서 인덕터 안쓰는거 대비 솔더브릿지 추가
캐패시터 24와 60중 고를 수 있게 수정 해야함
diag led가 빠졌는데 추가할지 확인해야함
병렬모터 spi 읽기 충돌 방지 대책 세워야 함
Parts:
- added JP2: SolderJumper_2_Open, Jumper:SolderJumper-2_P1.3mm_Open_TrianglePad1.0x1.5mm, symbol Jumper:SolderJumper_2_Open
- C58: value 22pF -> 22uF 22pF x 22uF ok; footprint Capacitor_SMD:C_0603_1608Metric -> Capacitor_SMD:C_0805_2012Metric
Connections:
- net PE5 is gone; now on net PE6: J69.6 (Pin_6)
- net +3.3ISO: now also JP2.1 (A)
- net GND: now also J69.7 (Pin_7)
- net PE6: no longer J69.7 (Pin_7)
- net at L2.1, PS1.8 (+VOUT): now also JP2.2 (B)
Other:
- moved on the sheet: C23, C24, C58, L2, R103, R104, U40
